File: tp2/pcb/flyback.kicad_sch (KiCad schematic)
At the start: 46 parts, among them J1 Conn_01x08_Socket, J2 Conn_01x08_Socket, Q1 2N2222, Q2 2N2907, Q3 TRBUZ80, Q4 BC547, U1 UC3526AN

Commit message: removed copied /flyback
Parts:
- removed D2: 6A20, symbol Device:D
- removed D5, D6: D, symbol Device:D
- added D2, D5: 6A20G, 6A20G:DIOAD1950W125L885D700, symbol 6A20G:6A20G
- added D6: MUR460, MUR460:DIOAD1990W125L900D530, symbol MUR460:MUR460
- C1, C2: footprint (none) -> TCLib:CP_2.50mm
- C10: value C -> 1n
- C11, C4, C5: footprint (none) -> TCLib:C_2.5mm
- C3: value 22p -> 22p-800V; footprint (none) -> TCLib:C_2.5mm
- C6: footprint Capacitor_THT:CP_Radial_D4.0mm_P1.50mm -> TCLib:CP_5.00mm
- D3, D4: footprint (none) -> LED_THT:LED_D1.8mm_W3.3mm_H2.4mm
- R1, R10, R11, R12, R13, R14, R2, R9: footprint (none) -> TCLib:R_0.125W
- R15: footprint TCLib:R_0.25W -> TCLib:R_0.125W
- R3: value 120k -> 120k-0.125W-800V; footprint (none) -> TCLib:R_0.125W
- R4: value 1k -> 1k-0.25W; footprint (none) -> TCLib:R_0.25W
- R5: value 22 -> 22-0.125W; footprint (none) -> TCLib:R_0.125W
- R6: value 470 -> 470-0.125W; footprint (none) -> TCLib:R_0.125W
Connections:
- net Vdrain: now also D6.A
- net Vout: now also D2.C
- net Vrealim: now also D5.C
- net at J2.8 (Pin_8), R7.1: now also D2.A
- net at C3.1, R3.2: now also D6.C
- net at J2.1 (Pin_1), R8.1: now also D5.A

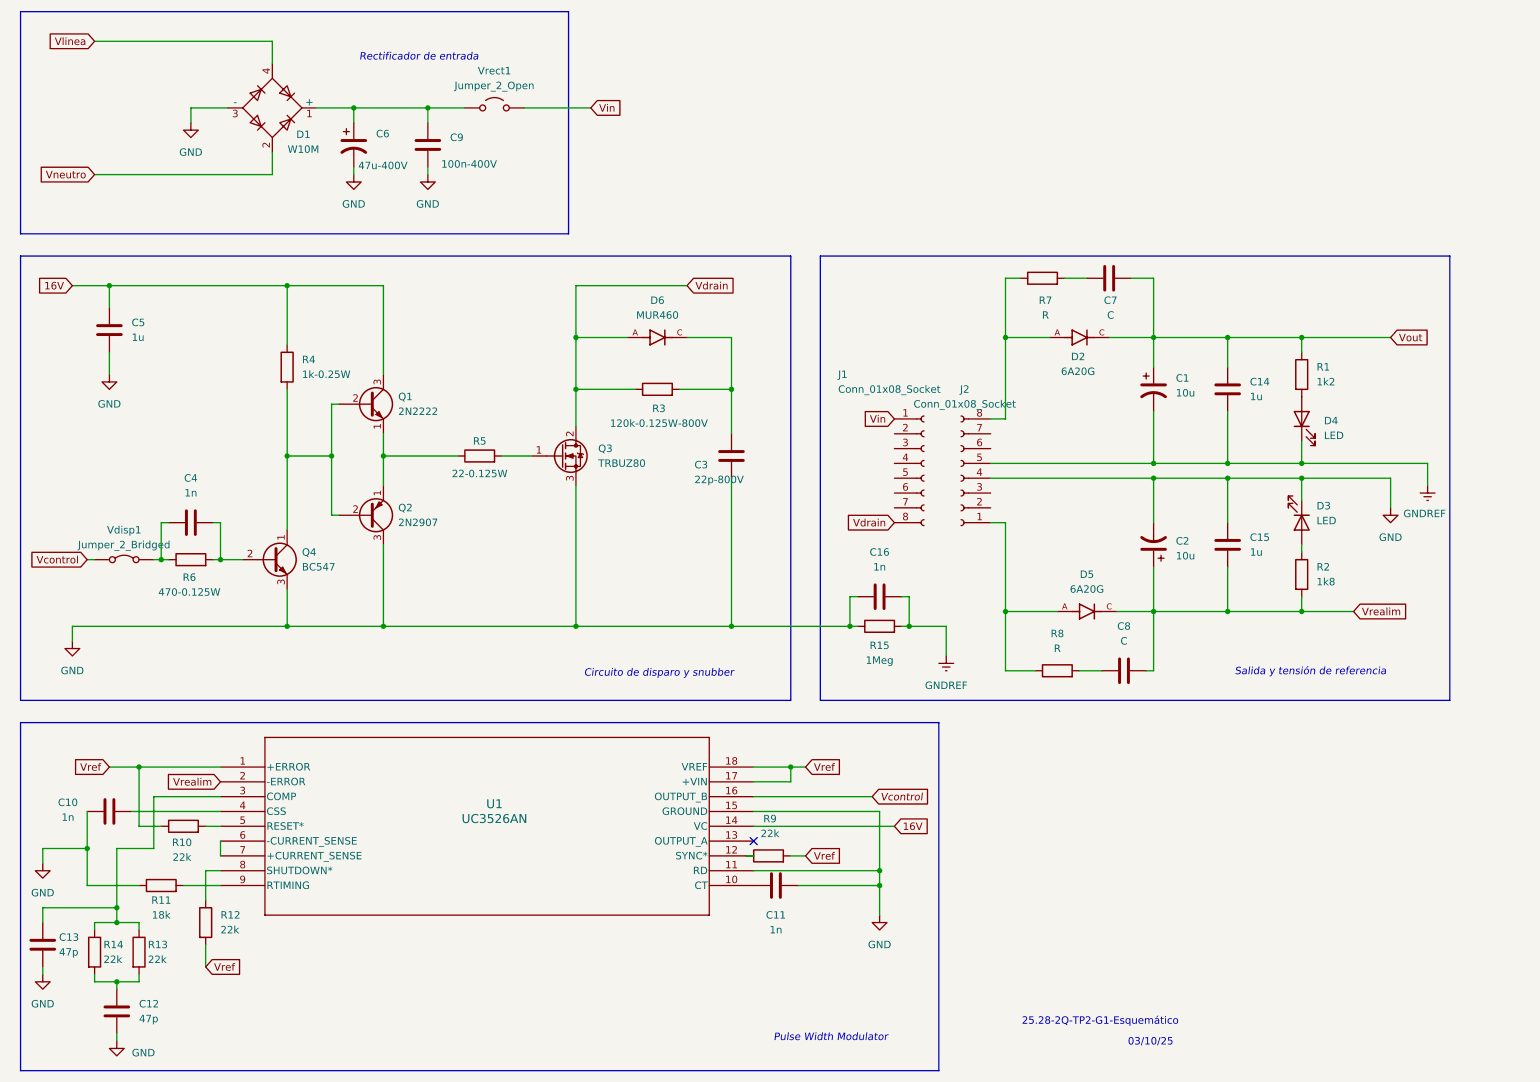
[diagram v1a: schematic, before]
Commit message: added almost all footprints to pcb
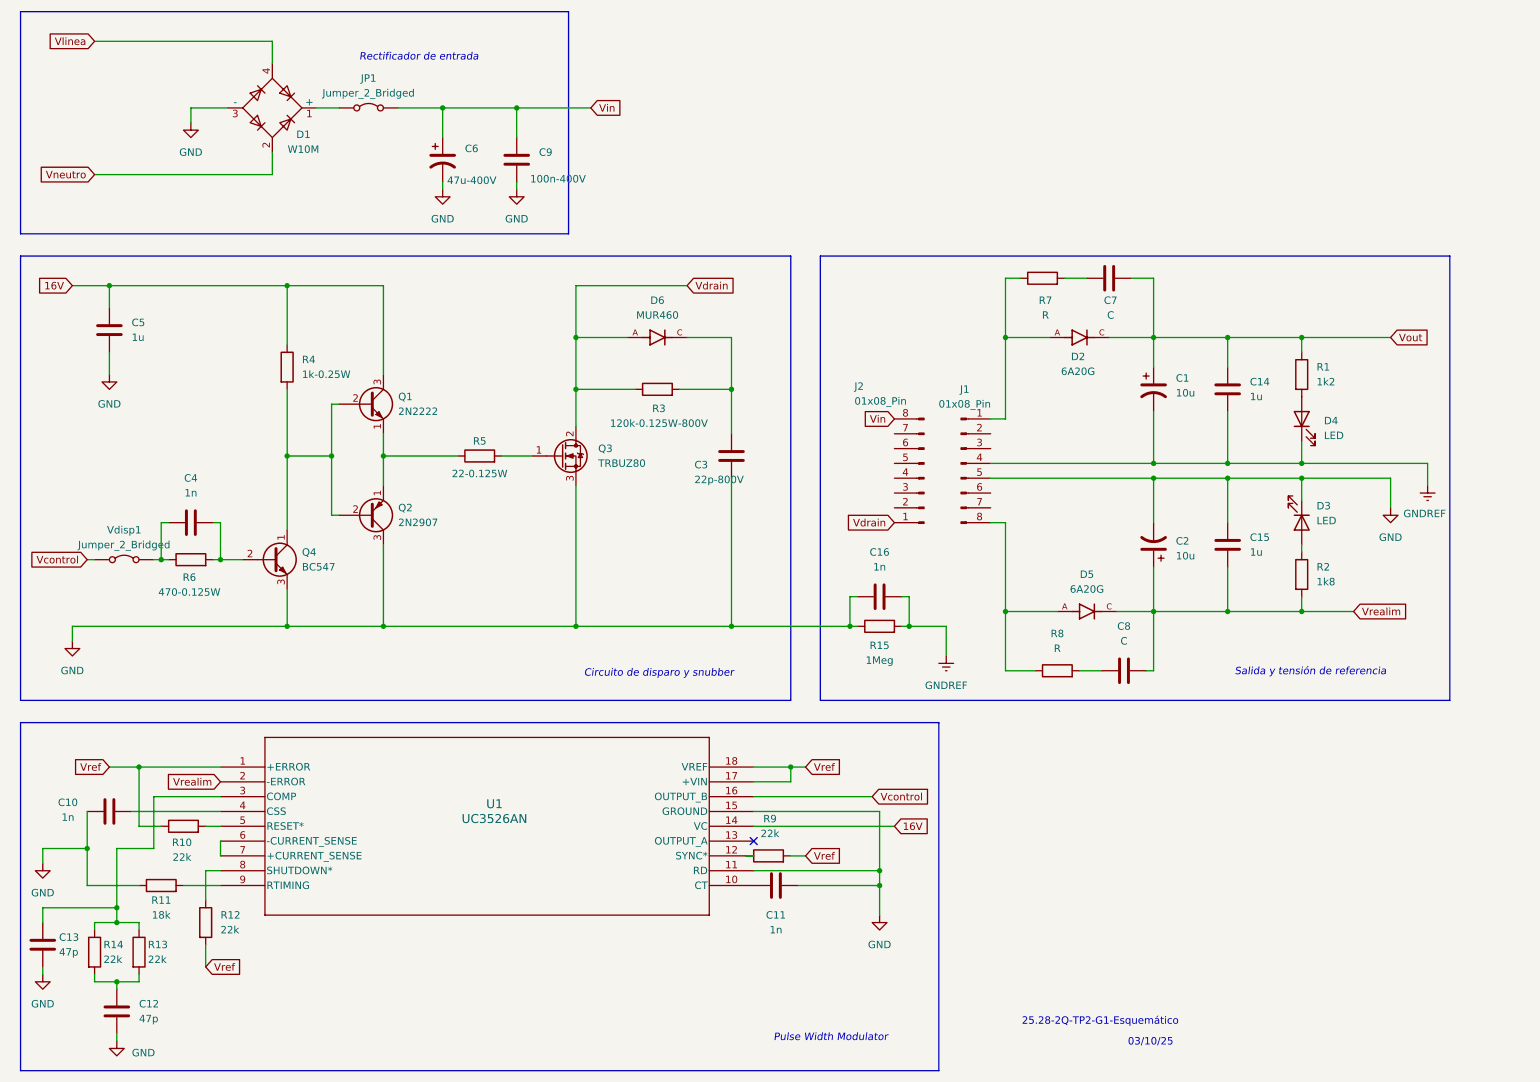
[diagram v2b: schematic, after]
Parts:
- removed J1, J2: Conn_01x08_Socket, Connector_Hirose:Hirose_DF13-08P-1.25DSA_1x08_P1.25mm_Vertical, symbol Connector:Conn_01x08_Socket
- removed Vrect1: Jumper_2_Open, symbol Jumper:Jumper_2_Open
- added J1, J2: 01x08_Pin, Connector_Hirose:Hirose_DF13-08P-1.25DSA_1x08_P1.25mm_Vertical, symbol Connector:Conn_01x08_Pin
- added JP1: Jumper_2_Bridged, Jumper:Jumper_Harwin_S1621_P10.9mm, symbol Jumper:Jumper_2_Bridged
- C10, C12, C13: footprint (none) -> TCLib:C_2.5mm
- Vdisp1: footprint (none) -> Jumper:Jumper_Harwin_S1621_P10.9mm
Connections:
- net GND: now also J1.5 (Pin_5)
- net GNDREF: now also J1.4 (Pin_4)
- net Vdrain: now also J2.1 (Pin_1)
- net Vin: now also C6.1, C9.1, J2.8 (Pin_8), JP1.2 (B)
- net at D2.A, R7.1: now also J1.1 (Pin_1)
- net at D5.A, R8.1: now also J1.8 (Pin_8)
- new net: D1.1 (+), JP1.1 (A)
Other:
- moved on the sheet: C6, C9

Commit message: hay que routear
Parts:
- removed J1, J2: 01x08_Pin, Connector_Hirose:Hirose_DF13-08P-1.25DSA_1x08_P1.25mm_Vertical, symbol Connector:Conn_01x08_Pin
- added J1, J2, J3, J4, J5, J6: Connector_2, Connector_AMASS:AMASS_XT30U-F_1x02_P5.0mm_Vertical, symbol TCLib:Connector_2
- C7, C8: value C -> C-50V; footprint (none) -> TCLib:C_2.5mm
- D6: footprint MUR460:DIOAD1990W125L900D530 -> MUR460(2):DIOAD1990W125L900D530
- R3: value 120k-0.125W-800V -> 58k-1W; footprint TCLib:R_0.125W -> TCLib:R_1W
- R7, R8: footprint (none) -> TCLib:R_0.125W
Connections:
- net GND: now also J5.1, J5.2
- net GNDREF: now also J4.1, J4.2
- net Vdrain: now also J2.1, J2.2
- net Vin: now also J1.1, J1.2
- net at D2.A, R7.1: now also J3.1, J3.2
- net at D5.A, R8.1: now also J6.1, J6.2
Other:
- note removed: "03/10/25"

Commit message: hay que routear2
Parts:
- added J7: Terminal_2, TCLib:Bornera_2_P5mm, symbol TCLib:Terminal_2
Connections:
- net 16V: now also J7.2; no longer U1.14 (VC)
- net GND: now also J7.1
- net Vref: now also U1.14 (VC)
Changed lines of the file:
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@@
 	)
 	(junction
+		(at 151.13 148.59)
+		(diameter 0)
+		(color 0 0 0 0)
+	)
+	(junction
 		(at 64.77 121.92)
 		(diameter 0)
@@
 	(wire
 		(pts
-			(xy 144.78 156.21) (xy 168.91 156.21)
+			(xy 144.78 156.21) (xy 151.13 156.21)
 		)
 		(stroke
@@
 	(wire
 		(pts
+			(xy 175.26 30.48) (xy 187.96 30.48)
+		)
+		(stroke
+			(width 0)
+			(type default)
+		)
+	)
+	(wire
+		(pts
 			(xy 254 97.79) (xy 254 101.6)
 		)
@@
 	(wire
 		(pts
+			(xy 187.96 30.48) (xy 187.96 35.56)
+		)
+		(stroke
+			(width 0)
+			(type default)
+		)
+	)
+	(wire
+		(pts
 			(xy 35.56 182.88) (xy 35.56 184.15)
 		)
@@
 	(wire
 		(pts
+			(xy 175.26 27.94) (xy 187.96 27.94)
+		)
+		(stroke
+			(width 0)
+			(type default)
+		)
+	)
+	(wire
+		(pts
 			(xy 226.06 97.79) (xy 226.06 104.14)
 		)
@@
 	(wire
 		(pts
+			(xy 151.13 148.59) (xy 151.13 156.21)
+		)
+		(stroke
+			(width 0)
+			(type default)
+		)
+	)
+	(wire
+		(pts
 			(xy 114.3 97.79) (xy 114.3 121.92)
 		)
@@
 		)
 	)
+	(global_label "16V"
+		(shape input)
+		(at 187.96 27.94 0)
+		(fields_autoplaced yes)
+		(effects
+			(font
+				(size 1.27 1.27)
+			)
+			(justify left)
+		)
+		(property "Intersheetrefs" "${INTERSHEET_REFS}"
+			(at 194.4528 27.94 0)
+			(effects
+				(font
+					(size 1.27 1.27)
+				)
+				(justify left)
+				(hide yes)
+			)
+		)
+	)
 	(global_label "Vout"
 		(shape input)
@@
 		)
 	)
-	(global_label "16V"
-		(shape input)
-		(at 168.91 156.21 0)
-		(fields_autoplaced yes)
-		(effects
-			(font
-				(size 1.27 1.27)
-			)
-			(justify left)
-		)
-		(property "Intersheetrefs" "${INTERSHEET_REFS}"
-			(at 175.4028 156.21 0)
-			(effects
-				(font
-					(size 1.27 1.27)
-				)
-				(justify left)
-				(hide yes)
-			)
-		)
-	)
 	(symbol
 		(lib_id "UC3526AN:UC3526AN")
@@
 	)
 	(symbol
+		(lib_id "TCLib:Terminal_2")
+		(at 172.72 29.21 0)
+		(unit 1)
+		(exclude_from_sim no)
+		(in_bom yes)
+		(on_board yes)
+		(dnp no)
+		(fields_autoplaced yes)
+		(property "Reference" "J7"
+			(at 172.847 21.59 0)
+			(effects
+				(font
+					(size 1.27 1.27)
+				)
+			)
+		)
+		(property "Value" "Terminal_2"
+			(at 172.847 24.13 0)
+			(effects
+				(font
+					(size 1.27 1.27)
+				)
+			)
+		)
+		(property "Footprint" "TCLib:Bornera_2_P5mm"
+			(at 172.212 24.892 0)
+			(effects
+				(font
+					(size 1.27 1.27)
+				)
+				(hide yes)
+			)
+		)
+		(property "Datasheet" ""
+			(at 172.72 29.21 0)
+			(effects
+				(font
+					(size 1.27 1.27)
+				)
+				(hide yes)
+			)
+		)
+		(property "Description" ""
+			(at 172.72 29.21 0)
+			(effects
+				(font
+					(size 1.27 1.27)
+				)
+				(hide yes)
+			)
+		)
+		(pin "2"
+		)
+		(pin "1"
+		)
+		(instances
+			(project ""
+				(path "/e1bc5ebe-0245-4788-8a28-7e348d07e41a"
+					(reference "J7")
+					(unit 1)
+				)
+			)
+		)
+	)
+	(symbol
 		(lib_id "Device:C")
 		(at 34.29 153.67 90)
@@
 					(unit 1)
 				)
+			)
+		)
+	)
+	(symbol
+		(lib_id "power:GND")
+		(at 187.96 35.56 0)
+		(unit 1)
+		(exclude_from_sim no)
+		(in_bom yes)
+		(on_board yes)
+		(dnp no)
+		(fields_autoplaced yes)
+		(property "Reference" "#PWR013"
+			(at 187.96 41.91 0)
+			(effects
+				(font
+					(size 1.27 1.27)
+				)
+				(hide yes)
+			)
+		)
+		(property "Value" "GND"
+			(at 187.96 40.64 0)
+			(effects
+				(font
+					(size 1.27 1.27)
+				)
+			)
+		)
+		(property "Footprint" ""
+			(at 187.96 35.56 0)
+			(effects
+				(font
+					(size 1.27 1.27)
+				)
+				(hide yes)
+			)
+		)
+		(property "Datasheet" ""
+			(at 187.96 35.56 0)
+			(effects
+				(font
+					(size 1.27 1.27)
+				)
+				(hide yes)
+			)
+		)
+		(property "Description" "Power symbol creates a global label with name \"GND\" , ground"
+			(at 187.96 35.56 0)
+			(effects
+				(font
+					(size 1.27 1.27)
+				)
+				(hide yes)
+			)
+		)
+		(pin "1"
+		)
+		(instances
+			(project ""
+				(path "/e1bc5ebe-0245-4788-8a28-7e348d07e41a"
+					(reference "#PWR013")
+					(unit 1)
+				)

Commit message: rutea facu
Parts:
- removed Q4: BC547, Package_TO_SOT_THT:TO-92_Inline, symbol Transistor_BJT:BC547
- added J8: Terminal_2, TCLib:Bornera_2_P5mm, symbol TCLib:Terminal_2
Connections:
- net Vcontrol: now also U1.13 (OUTPUT_A); no longer U1.16 (OUTPUT_B)
- net Vlinea: now also J8.2
- net Vneutro: now also J8.1
- net Vrealim: now also U1.14 (VC), U1.17 (+VIN); no longer U1.2 (-ERROR)
- net Vref: no longer U1.14 (VC), U1.17 (+VIN)
- net at Q1.2 (B), Q2.2 (B), R4.2: now also C4.2, R6.2

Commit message: ya rutie la flybuk
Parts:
- added R16, R20: 10k, TCLib:R_0.25W, symbol TCLib:R
- added R17: 3k9, TCLib:R_0.25W, symbol TCLib:R
- added RV1: 10k, TCLib:RV_Preset_multivuelta_10mm_5mm, symbol TCLib:R_Potentiometer
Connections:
- net GND: now also R17.2, R20.2
- net Vrealim: now also R16.2
- net Vref: now also RV1.3; no longer U1.1 (+ERROR)
- net Vrealim': now reaches U1.2 (-ERROR)
- net Vrealim': now also R16.1, R17.1
- new net Vref': R20.1, RV1.1, RV1.2, U1.1 (+ERROR)

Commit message: por si me muero
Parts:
- removed C12, C13: 47p, TCLib:C_2.5mm, symbol Device:C
- removed D6: MUR460, MUR460(2):DIOAD1990W125L900D530, symbol MUR460:MUR460
- removed JP1, Vdisp1: Jumper_2_Bridged, Jumper:Jumper_Harwin_S1621_P10.9mm, symbol Jumper:Jumper_2_Bridged
- added C12, C13: 47p, TCLib:C_5mm, symbol TCLib:C
- added C17: 100n, TCLib:C_2.5mm, symbol TCLib:C
- added D6: MUR160, MUR160:DIOAD1300W80L670D310, symbol MUR160:MUR160
- added J10, J9: Connector_2, TCLib:PinHeader_1x02_P2.54mm_Vertical, symbol TCLib:Connector_2
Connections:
- net GND: now also C12.2, C13.2, C17.1
- net Vcontrol: now also J9.1
- net Vdrain: now also D6.A
- net Vin: now also J10.2
- net Vrealim: now also C17.2
- net at R13.1, R14.1, U1.3 (COMP): now also C13.1
- net at D1.1 (+): now also J10.1
- net at R13.2, R14.2: now also C12.1
- net at C4.1, R6.1: now also J9.2
- net at C3.1, R3.2: now also D6.C

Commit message: listo el routeo
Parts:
- added HS1: Heatsink, Heatsink:Heatsink_Stonecold_HS-S02_13.21x9.53mm, symbol Mechanical:Heatsink
- J1, J2, J3, J4, J5, J6: footprint Connector_AMASS:AMASS_XT30U-F_1x02_P5.0mm_Vertical -> TCLib:PinHeader_1x03_P2.54mm_Vertical
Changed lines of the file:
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@@
 			)
 		)
-		(property "Footprint" "Connector_AMASS:AMASS_XT30U-F_1x02_P5.0mm_Vertical"
+		(property "Footprint" "TCLib:PinHeader_1x03_P2.54mm_Vertical"
 			(at 183.388 103.378 0)
 			(effects
@@
 			)
 		)
-		(property "Footprint" "Connector_AMASS:AMASS_XT30U-F_1x02_P5.0mm_Vertical"
+		(property "Footprint" "TCLib:PinHeader_1x03_P2.54mm_Vertical"
 			(at 170.942 98.552 0)
 			(effects
@@
 			)
 		)
-		(property "Footprint" "Connector_AMASS:AMASS_XT30U-F_1x02_P5.0mm_Vertical"
+		(property "Footprint" "TCLib:PinHeader_1x03_P2.54mm_Vertical"
 			(at 183.388 110.998 0)
 			(effects
@@
 			)
 		)
-		(property "Footprint" "Connector_AMASS:AMASS_XT30U-F_1x02_P5.0mm_Vertical"
+		(property "Footprint" "TCLib:PinHeader_1x03_P2.54mm_Vertical"
 			(at 183.388 97.028 0)
 			(effects
@@
 			)
 		)
-		(property "Footprint" "Connector_AMASS:AMASS_XT30U-F_1x02_P5.0mm_Vertical"
+		(property "Footprint" "TCLib:PinHeader_1x03_P2.54mm_Vertical"
 			(at 183.388 89.408 0)
 			(effects
@@
 	)
 	(symbol
+		(lib_id "Mechanical:Heatsink")
+		(at 107.95 86.36 0)
+		(unit 1)
+		(exclude_from_sim no)
+		(in_bom yes)
+		(on_board yes)
+		(dnp no)
+		(fields_autoplaced yes)
+		(property "Reference" "HS1"
+			(at 111.76 83.1849 0)
+			(effects
+				(font
+					(size 1.27 1.27)
+				)
+				(justify left)
+			)
+		)
+		(property "Value" "Heatsink"
+			(at 111.76 85.7249 0)
+			(effects
+				(font
+					(size 1.27 1.27)
+				)
+				(justify left)
+			)
+		)
+		(property "Footprint" "Heatsink:Heatsink_Stonecold_HS-S02_13.21x9.53mm"
+			(at 108.2548 86.36 0)
+			(effects
+				(font
+					(size 1.27 1.27)
+				)
+				(hide yes)
+			)
+		)
+		(property "Datasheet" "~"
+			(at 108.2548 86.36 0)
+			(effects
+				(font
+					(size 1.27 1.27)
+				)
+				(hide yes)
+			)
+		)
+		(property "Description" "Heatsink"
+			(at 107.95 86.36 0)
+			(effects
+				(font
+					(size 1.27 1.27)
+				)
+				(hide yes)
+			)
+		)
+		(instances
+			(project ""
+				(path "/e1bc5ebe-0245-4788-8a28-7e348d07e41a"
+					(reference "HS1")
+					(unit 1)
+				)
+			)
+		)
+	)
+	(symbol
 		(lib_id "TCLib:2N2907")
 		(at 81.28 102.87 0)
@@
 			)
 		)
-		(property "Footprint" "Connector_AMASS:AMASS_XT30U-F_1x02_P5.0mm_Vertical"
+		(property "Footprint" "TCLib:PinHeader_1x03_P2.54mm_Vertical"
 			(at 170.942 80.772 0)
 			(effects
